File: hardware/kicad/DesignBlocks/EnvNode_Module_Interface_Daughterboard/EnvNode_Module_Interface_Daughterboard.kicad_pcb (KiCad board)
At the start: 2 copper layers, 2 parts, among them J1 Conn_02x04_Odd_Even, J2 Conn_02x04_Odd_Even

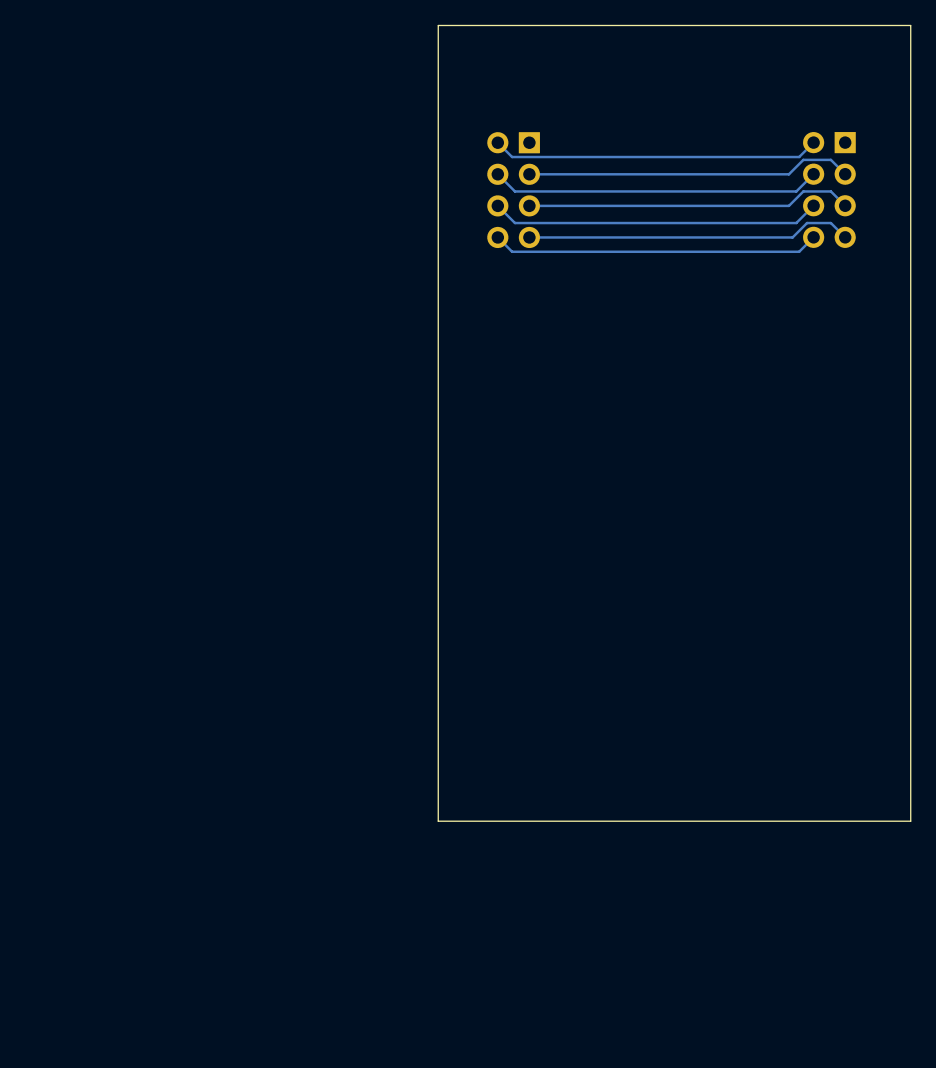
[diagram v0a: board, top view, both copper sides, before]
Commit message: Updated EnvNode Modules Interfaces
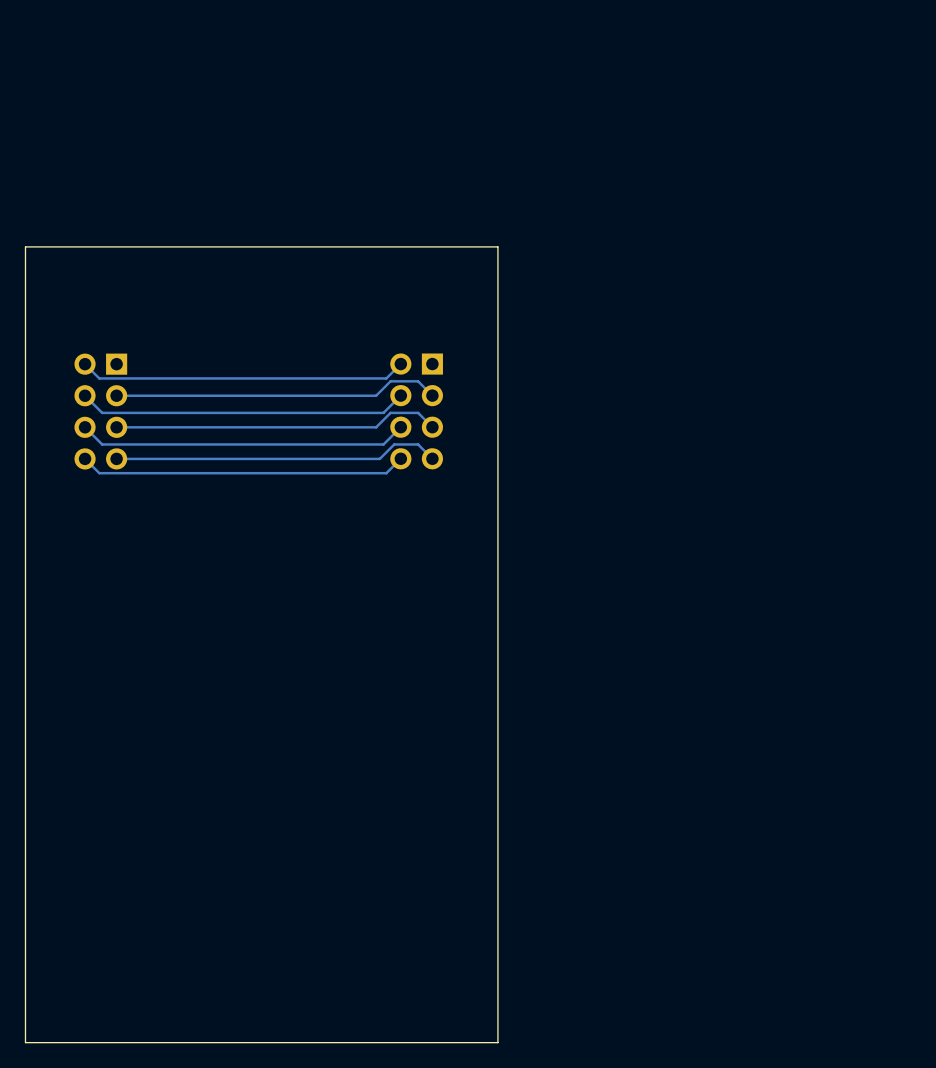
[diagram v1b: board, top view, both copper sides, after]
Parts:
- moved J1 37.7 mm to (150.6, 62.2)
- moved J2 37.7 mm to (125.2, 62.2)
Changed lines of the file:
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@@
 	(footprint "EnvNode-Footprints:PinSocket_2x04_P2.54mm_Vertical_Bottom"
 		(layer "B.Cu")
-		(at 183.77 44.36 180)
+		(at 150.57 62.17 180)
 		(descr "Through hole straight socket strip, 2x04, 2.54mm pitch, double rows (from Kicad 4.0.7), script generated")
 		(tags "Through hole socket strip THT 2x04 2.54mm double row")
@@
 		(sheetname "/")
 		(sheetfile "EnvNode_Module_Interface_Daughterboard.kicad_sch")
+		(units
+			(unit
+				(name "A")
+				(pins "1" "3" "5" "7" "2" "4" "6" "8")
+			)
+		)
 		(attr through_hole)
 		(duplicate_pad_numbers_are_jumpers no)
@@
 	(footprint "EnvNode-Footprints:PinSocket_2x04_P2.54mm_Vertical_Bottom"
 		(layer "B.Cu")
-		(at 158.37 44.37 180)
+		(at 125.17 62.18 180)
 		(descr "Through hole straight socket strip, 2x04, 2.54mm pitch, double rows (from Kicad 4.0.7), script generated")
 		(tags "Through hole socket strip THT 2x04 2.54mm double row")
@@
 		(sheetname "/")
 		(sheetfile "EnvNode_Module_Interface_Daughterboard.kicad_sch")
+		(units
+			(unit
+				(name "A")
+				(pins "1" "3" "5" "7" "2" "4" "6" "8")
+			)
+		)
 		(attr through_hole)
 		(duplicate_pad_numbers_are_jumpers no)
@@
 	)
 	(gr_rect
-		(start 153.58 34.94)
-		(end 191.58 98.94)
+		(start 120.38 52.75)
+		(end 158.38 116.75)
 		(stroke
 			(width 0.1)
@@
 	)
 	(segment
-		(start 182.945686 45.75)
-		(end 181.785686 46.91)
+		(start 149.41 63.33)
+		(end 126.32 63.33)
+		(width 0.2)
+		(layer "B.Cu")
+		(net "/24V")
+	)
+	(segment
+		(start 126.32 63.33)
+		(end 125.17 62.18)
+		(width 0.2)
+		(layer "B.Cu")
+		(net "/24V")
+	)
+	(segment
+		(start 150.57 62.17)
+		(end 149.41 63.33)
+		(width 0.2)
+		(layer "B.Cu")
+		(net "/24V")
+	)
+	(segment
+		(start 149.745686 63.56)
+		(end 148.585686 64.72)
 		(width 0.2)
 		(layer "B.Cu")
@@
 	)
 	(segment
-		(start 186.31 46.9)
-		(end 185.16 45.75)
+		(start 153.11 64.71)
+		(end 151.96 63.56)
 		(width 0.2)
 		(layer "B.Cu")
@@
 	)
 	(segment
-		(start 185.16 45.75)
-		(end 182.945686 45.75)
+		(start 151.96 63.56)
+		(end 149.745686 63.56)
 		(width 0.2)
 		(layer "B.Cu")
@@
 	)
 	(segment
-		(start 181.785686 46.91)
-		(end 160.91 46.91)
+		(start 148.585686 64.72)
+		(end 127.71 64.72)
 		(width 0.2)
 		(layer "B.Cu")
@@
 	)
 	(segment
-		(start 182.61 45.52)
-		(end 159.52 45.52)
-		(width 0.2)
-		(layer "B.Cu")
-		(net "/24V")
-	)
-	(segment
-		(start 183.77 44.36)
-		(end 182.61 45.52)
-		(width 0.2)
-		(layer "B.Cu")
-		(net "/24V")
-	)
-	(segment
-		(start 159.52 45.52)
-		(end 158.37 44.37)
-		(width 0.2)
-		(layer "B.Cu")
-		(net "/24V")
-	)
-	(segment
-		(start 185.16 48.29)
-		(end 182.945686 48.29)
+		(start 126.55 66.1)
+		(end 149.18 66.1)
+		(width 0.2)
+		(layer "B.Cu")
+		(net "/5V")
+	)
+	(segment
+		(start 149.18 66.1)
+		(end 150.57 64.71)
+		(width 0.2)
+		(layer "B.Cu")
+		(net "/5V")
+	)
+	(segment
+		(start 125.17 64.72)
+		(end 126.55 66.1)
+		(width 0.2)
+		(layer "B.Cu")
+		(net "/5V")
+	)
+	(segment
+		(start 148.585686 67.26)
+		(end 127.71 67.26)
 		(width 0.2)
 		(layer "B.Cu")
@@
 	)
 	(segment
-		(start 181.785686 49.45)
-		(end 160.91 49.45)
+		(start 149.745686 66.1)
+		(end 148.585686 67.26)
 		(width 0.2)
 		(layer "B.Cu")
@@
 	)
 	(segment
-		(start 182.945686 48.29)
-		(end 181.785686 49.45)
+		(start 153.11 67.25)
+		(end 151.96 66.1)
 		(width 0.2)
 		(layer "B.Cu")
@@
 	)
 	(segment
-		(start 186.31 49.44)
-		(end 185.16 48.29)
+		(start 151.96 66.1)
+		(end 149.745686 66.1)
 		(width 0.2)
 		(layer "B.Cu")
@@
 	)
 	(segment
-		(start 182.38 50.83)
-		(end 183.77 49.44)
+		(start 126.55 68.64)
+		(end 149.18 68.64)
 		(width 0.2)
 		(layer "B.Cu")
@@
 	)
 	(segment
-		(start 159.75 50.83)
-		(end 182.38 50.83)
+		(start 125.17 67.26)
+		(end 126.55 68.64)
 		(width 0.2)
 		(layer "B.Cu")
@@
 	)
 	(segment
-		(start 158.37 49.45)
-		(end 159.75 50.83)
+		(start 149.18 68.64)
+		(end 150.57 67.25)
 		(width 0.2)
 		(layer "B.Cu")
@@
 	)
 	(segment
-		(start 160.945 51.955)
-		(end 160.915 51.985)
+		(start 150.04 68.64)
+		(end 148.88 69.8)
 		(width 0.2)
 		(layer "B.Cu")
@@
 	)
 	(segment
-		(start 183.24 50.83)
-		(end 182.08 51.99)
+		(start 151.96 68.64)
+		(end 150.04 68.64)
 		(width 0.2)
 		(layer "B.Cu")
@@
 	)
 	(segment
-		(start 185.16 50.83)
-		(end 183.24 50.83)
+		(start 153.11 69.79)
+		(end 151.96 68.64)
 		(width 0.2)
 		(layer "B.Cu")
@@
 	)
 	(segment
-		(start 182.08 51.99)
-		(end 160.91 51.99)
+		(start 148.88 69.8)
+		(end 127.71 69.8)
 		(width 0.2)
 		(layer "B.Cu")
@@
 	)
 	(segment
-		(start 186.31 51.98)
-		(end 185.16 50.83)
+		(start 127.745 69.765)
+		(end 127.715 69.795)
 		(width 0.2)
 		(layer "B.Cu")
@@
 	)
 	(segment
-		(start 159.52 53.14)
-		(end 182.61 53.14)
+		(start 126.32 70.95)
+		(end 149.41 70.95)
 		(width 0.2)
 		(layer "B.Cu")
@@
 	)
 	(segment
-		(start 182.61 53.14)
-		(end 183.77 51.98)
+		(start 125.17 69.8)
+		(end 126.32 70.95)
 		(width 0.2)
 		(layer "B.Cu")
@@
 	)
 	(segment
-		(start 158.37 51.99)
-		(end 159.52 53.14)
+		(start 149.41 70.95)
+		(end 150.57 69.79)
 		(width 0.2)
 		(layer "B.Cu")
 		(net "/GPIO2")
-	)
-	(segment
-		(start 159.75 48.29)
-		(end 182.38 48.29)
-		(width 0.2)
-		(layer "B.Cu")
-		(net "/5V")
-	)
-	(segment
-		(start 182.38 48.29)
-		(end 183.77 46.9)
-		(width 0.2)
-		(layer "B.Cu")
-		(net "/5V")
-	)
-	(segment
-		(start 158.37 46.91)
-		(end 159.75 48.29)
-		(width 0.2)
-		(layer "B.Cu")
-		(net "/5V")
 	)
 	(group ""
 		(lib_id "EnvNodeDesignBlocks:EnvNode_Module_Interface_Daughterboard")
-		(members "1fd6a4f9-d9be-4ef3-b1a7-e42ad22bb043" "abdbb613-462b-435e-91c2-9466207fe9f7")
+		(members "003c8b3b-0cc0-4f67-8da6-253e704f713e" "20a52997-14fe-436f-bdd1-ef99f9ea5cb0"
+			"25fc41ee-85c9-4d1f-837e-c3a408cf8530" "27b103ff-75e2-4b95-bd9b-b2b5fb7b0bcc"
+			"2e85fa91-8c85-413a-9c90-b0922fc3903b" "311a5afa-0adf-4ce5-af4e-7cec1efb5213"
+			"325fefb4-229a-46ed-a001-fe03ed8c92be" "35f0d4e1-5149-4e61-b9af-0e3323bdb0ee"
+			"3b0c9218-94d9-4412-8646-fb64b718ca47" "403aaa93-570c-41b4-9827-5634da065eff"
+			"4d4a02d8-5c1d-4949-97fe-35cefe91e51c" "5977dff8-2807-4060-a16a-2497edaa406c"
+			"5ea8b983-cb4a-4d04-b60f-8b2faee96f4a" "606a5fd7-cd9d-45b4-a23e-1dbd1075a541"
+			"68831de7-b0ea-47d7-adb3-1deaef367dac" "779ad242-7e2d-4d10-a574-9f3f6ecafa9b"
+			"8e0ae5a5-0e10-40ef-9955-1efe452e64a0" "91f851c4-1807-4809-9693-9c5c8d87613e"
+			"a5ad8ac8-3135-4820-b761-2a712a52b5ea" "aefb7aec-4157-42f6-8b12-34bf2ad256ce"
+			"bfdd481a-1cf6-4ece-8b3d-b9baf0202873" "c6593a78-d2fd-4ab5-984c-de106519d3c5"
+			"ccccd795-9db6-4b6b-a7bd-4a0544e10919" "cd3d5e50-fc66-4257-8cce-fc27aae9d1d8"
+			"dda50c7f-b302-4664-add9-b7aa22e9df28" "e039634c-3f90-4948-8611-ca6acd05a0f8"
+			"fc1146ef-dee4-4a48-a08f-19b26d9fa546" "fdf5f8f9-0d8b-4028-95a0-044476252cce"
+		)
 	)
 	(embedded_fonts no)

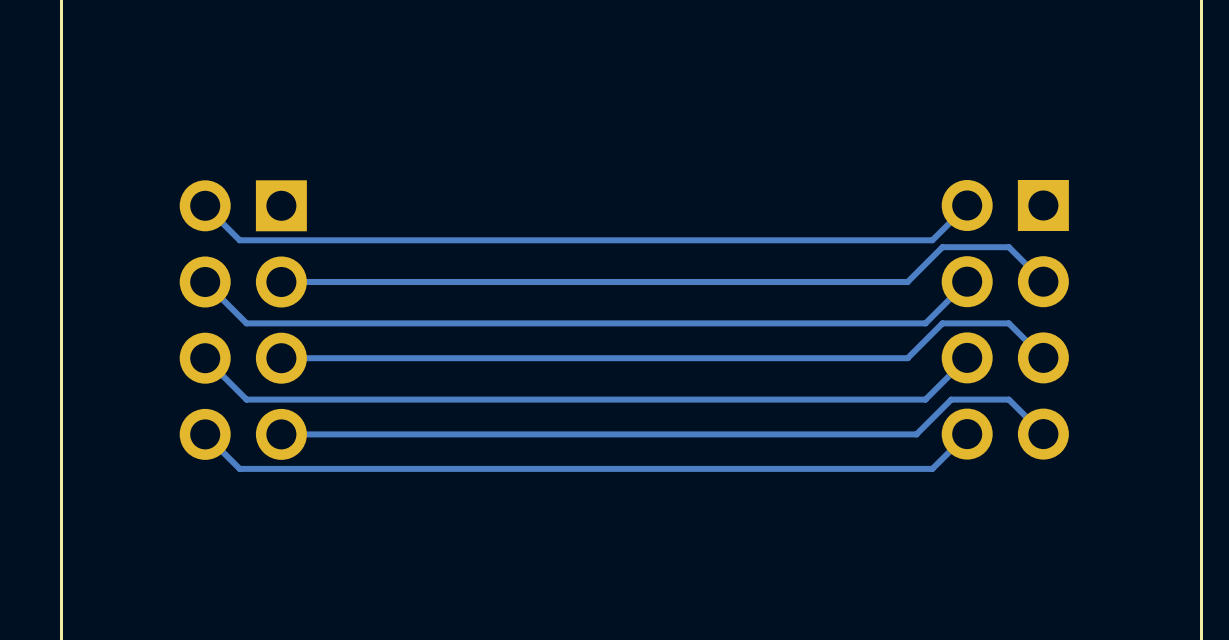
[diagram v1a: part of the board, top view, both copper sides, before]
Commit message: docs(hardware): document daughterboard module interface design block
- document the module-side connector design block and update workflow
- record standardized pinout and 25.40 mm connector spacing
- document Bottom footprints and routing-width baseline
- add the design block to the central hardware specification
- create the hardware documentation index
- update design block metadata
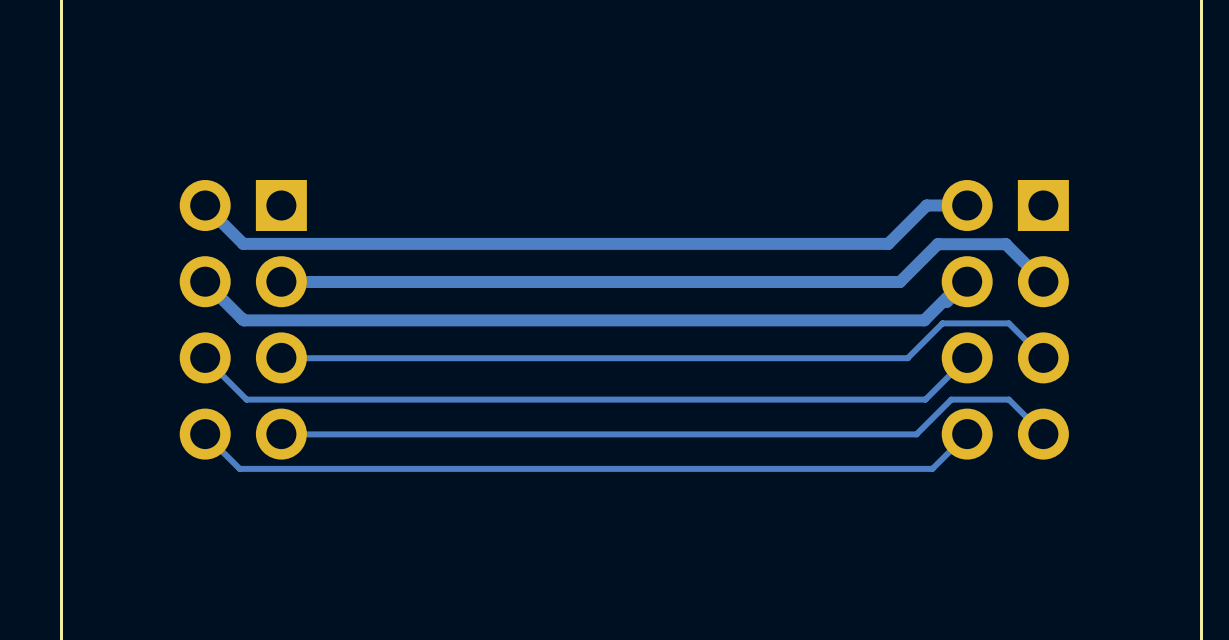
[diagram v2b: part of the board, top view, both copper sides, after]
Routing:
- net /5V: track 26.5 -> 27.4 mm
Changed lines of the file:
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@@
 	(footprint "EnvNode-Footprints:PinSocket_2x04_P2.54mm_Vertical_Bottom"
 		(layer "B.Cu")
-		(at 125.17 62.18 180)
+		(at 125.17 62.17 180)
 		(descr "Through hole straight socket strip, 2x04, 2.54mm pitch, double rows (from Kicad 4.0.7), script generated")
 		(tags "Through hole socket strip THT 2x04 2.54mm double row")
@@
 	)
 	(segment
-		(start 149.41 63.33)
-		(end 126.32 63.33)
-		(width 0.2)
+		(start 126.44 63.45)
+		(end 147.94 63.45)
+		(width 0.4)
 		(layer "B.Cu")
 		(net "/24V")
 	)
 	(segment
-		(start 126.32 63.33)
-		(end 125.17 62.18)
-		(width 0.2)
+		(start 125.17 62.18)
+		(end 126.44 63.45)
+		(width 0.4)
 		(layer "B.Cu")
 		(net "/24V")
 	)
 	(segment
-		(start 150.57 62.17)
-		(end 149.41 63.33)
-		(width 0.2)
+		(start 147.94 63.45)
+		(end 149.22 62.17)
+		(width 0.4)
 		(layer "B.Cu")
 		(net "/24V")
 	)
 	(segment
-		(start 149.745686 63.56)
-		(end 148.585686 64.72)
-		(width 0.2)
+		(start 149.22 62.17)
+		(end 150.57 62.17)
+		(width 0.4)
+		(layer "B.Cu")
+		(net "/24V")
+	)
+	(segment
+		(start 149.59 63.46)
+		(end 148.33 64.72)
+		(width 0.4)
 		(layer "B.Cu")
 		(net "/3V3")
 	)
 	(segment
+		(start 151.86 63.46)
+		(end 149.59 63.46)
+		(width 0.4)
+		(layer "B.Cu")
+		(net "/3V3")
+	)
+	(segment
+		(start 148.33 64.72)
+		(end 127.71 64.72)
+		(width 0.4)
+		(layer "B.Cu")
+		(net "/3V3")
+	)
+	(segment
 		(start 153.11 64.71)
-		(end 151.96 63.56)
-		(width 0.2)
+		(end 151.86 63.46)
+		(width 0.4)
 		(layer "B.Cu")
 		(net "/3V3")
 	)
 	(segment
-		(start 151.96 63.56)
-		(end 149.745686 63.56)
-		(width 0.2)
-		(layer "B.Cu")
-		(net "/3V3")
-	)
-	(segment
-		(start 148.585686 64.72)
-		(end 127.71 64.72)
-		(width 0.2)
-		(layer "B.Cu")
-		(net "/3V3")
-	)
-	(segment
-		(start 126.55 66.1)
-		(end 149.18 66.1)
-		(width 0.2)
-		(layer "B.Cu")
-		(net "/5V")
-	)
-	(segment
-		(start 149.18 66.1)
+		(start 150.42858 64.71)
 		(end 150.57 64.71)
-		(width 0.2)
+		(width 0.4)
+		(layer "B.Cu")
+		(net "/5V")
+	)
+	(segment
+		(start 126.39 65.94)
+		(end 126.4 65.94)
+		(width 0.4)
+		(layer "B.Cu")
+		(net "/5V")
+	)
+	(segment
+		(start 126.46 66)
+		(end 149.13858 66)
+		(width 0.4)
+		(layer "B.Cu")
+		(net "/5V")
+	)
+	(segment
+		(start 126.4 65.94)
+		(end 126.46 66)
+		(width 0.4)
+		(layer "B.Cu")
+		(net "/5V")
+	)
+	(segment
+		(start 149.13858 66)
+		(end 150.42858 64.71)
+		(width 0.4)
+		(layer "B.Cu")
+		(net "/5V")
+	)
+	(segment
+		(start 150.57 64.71)
+		(end 149.89 65.39)
+		(width 0.4)
 		(layer "B.Cu")
 		(net "/5V")
@@
 	(segment
 		(start 125.17 64.72)
-		(end 126.55 66.1)
-		(width 0.2)
+		(end 126.39 65.94)
+		(width 0.4)
 		(layer "B.Cu")
 		(net "/5V")
@@
 	(group ""
 		(lib_id "EnvNodeDesignBlocks:EnvNode_Module_Interface_Daughterboard")
-		(members "003c8b3b-0cc0-4f67-8da6-253e704f713e" "20a52997-14fe-436f-bdd1-ef99f9ea5cb0"
-			"25fc41ee-85c9-4d1f-837e-c3a408cf8530" "27b103ff-75e2-4b95-bd9b-b2b5fb7b0bcc"
-			"2e85fa91-8c85-413a-9c90-b0922fc3903b" "311a5afa-0adf-4ce5-af4e-7cec1efb5213"
-			"325fefb4-229a-46ed-a001-fe03ed8c92be" "35f0d4e1-5149-4e61-b9af-0e3323bdb0ee"
+		(members "162b46fc-5f49-40aa-b153-07c8de5603cc" "183b4383-7708-4d10-a2b5-1bd07630ccc6"
+			"27b103ff-75e2-4b95-bd9b-b2b5fb7b0bcc" "2e85fa91-8c85-413a-9c90-b0922fc3903b"
+			"311a5afa-0adf-4ce5-af4e-7cec1efb5213" "325fefb4-229a-46ed-a001-fe03ed8c92be"
+			"3521980d-b48c-4724-911e-0e3342699021" "35f0d4e1-5149-4e61-b9af-0e3323bdb0ee"
 			"3b0c9218-94d9-4412-8646-fb64b718ca47" "403aaa93-570c-41b4-9827-5634da065eff"
-			"4d4a02d8-5c1d-4949-97fe-35cefe91e51c" "5977dff8-2807-4060-a16a-2497edaa406c"
+			"4f70ed5f-6fcf-4063-8237-5aba9da55dfd" "5977dff8-2807-4060-a16a-2497edaa406c"
 			"5ea8b983-cb4a-4d04-b60f-8b2faee96f4a" "606a5fd7-cd9d-45b4-a23e-1dbd1075a541"
-			"68831de7-b0ea-47d7-adb3-1deaef367dac" "779ad242-7e2d-4d10-a574-9f3f6ecafa9b"
-			"8e0ae5a5-0e10-40ef-9955-1efe452e64a0" "91f851c4-1807-4809-9693-9c5c8d87613e"
-			"a5ad8ac8-3135-4820-b761-2a712a52b5ea" "aefb7aec-4157-42f6-8b12-34bf2ad256ce"
-			"bfdd481a-1cf6-4ece-8b3d-b9baf0202873" "c6593a78-d2fd-4ab5-984c-de106519d3c5"
-			"ccccd795-9db6-4b6b-a7bd-4a0544e10919" "cd3d5e50-fc66-4257-8cce-fc27aae9d1d8"
-			"dda50c7f-b302-4664-add9-b7aa22e9df28" "e039634c-3f90-4948-8611-ca6acd05a0f8"
-			"fc1146ef-dee4-4a48-a08f-19b26d9fa546" "fdf5f8f9-0d8b-4028-95a0-044476252cce"
-		)
-	)
+			"6c14f8f3-e55b-4876-9ff8-6adb742b55ff" "6d3be3b7-4302-41e0-b177-1e0fe2c28eb3"
+			"74459c1a-9a4b-4b86-a0bf-b54d6319a41c" "779ad242-7e2d-4d10-a574-9f3f6ecafa9b"
+			"79370e78-36df-45fb-a9c8-488a4e0bf79c" "7de93003-14cd-422f-a24e-b885d8df8f13"
+			"8de5ac5a-ae97-42c0-a103-4452e2b74c8d" "8e0ae5a5-0e10-40ef-9955-1efe452e64a0"
+			"8f957ed0-08d1-4c30-bd80-c9dd92358162" "91f851c4-1807-4809-9693-9c5c8d87613e"
+			"a5ad8ac8-3135-4820-b761-2a712a52b5ea" "c6593a78-d2fd-4ab5-984c-de106519d3c5"
+			"c8f7e4c5-9ad9-4aea-875a-1bace808fe69" "d0ae9105-5921-4718-8c2a-e73ed8689807"
+			"d4ab6311-06e5-49d8-9813-c69650a0fe09" "dda50c7f-b302-4664-add9-b7aa22e9df28"
+			"ea36d5b6-7e7b-47f9-a6bc-da2f64476058" "fdf5f8f9-0d8b-4028-95a0-044476252cce"
+		)
+	)
